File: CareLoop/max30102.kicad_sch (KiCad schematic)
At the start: 4 parts, among them U2 MAX30102

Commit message: updated version
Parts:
- added C21, C22: 4.7u, Capacitor_SMD:C_0603_1608Metric_Pad1.08x0.95mm_HandSolder, symbol Device:C
- added C23: 100n, Capacitor_SMD:C_0603_1608Metric_Pad1.08x0.95mm_HandSolder, symbol Device:C
- added C24: 1u, Capacitor_SMD:C_0603_1608Metric_Pad1.08x0.95mm_HandSolder, symbol Device:C
- added R8: 10k, Resistor_SMD:R_0603_1608Metric_Pad0.98x0.95mm_HandSolder, symbol Device:R
- added U1: MCP1727-1802xMF, Package_DFN_QFN:DFN-8-1EP_3x3mm_P0.65mm_EP1.55x2.4mm, symbol Regulator_Linear:MCP1727-1802xMF
- C3: value 1u -> 10u
- renumbered JP1 to JP1_MAX30102
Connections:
- net GND: now also C21.2, C22.2, C23.2, C24.2, U1.4 (GND), U1.9 (GND)
- net at C15.1, C3.1, JP1_MAX30102.1 (A)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: now also C22.1, C23.1, R8.1, U1.1 (Vin), U1.2 (Vin), U1.3 (~{SHDN}); no longer U2.11 (VDD)
- net MAX_INT: now reaches U2.13 (~{INT})
- net MAX_INT: now also R8.2
- new net: C21.1, C24.1, U1.8 (Vout), U2.11 (VDD)
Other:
- moved on the sheet: JP1_MAX30102

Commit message: WP: update Schematics
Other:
- moved on the sheet: C15, C21, C22, C23, C24, C3, JP1_MAX30102, R8, U1, U2

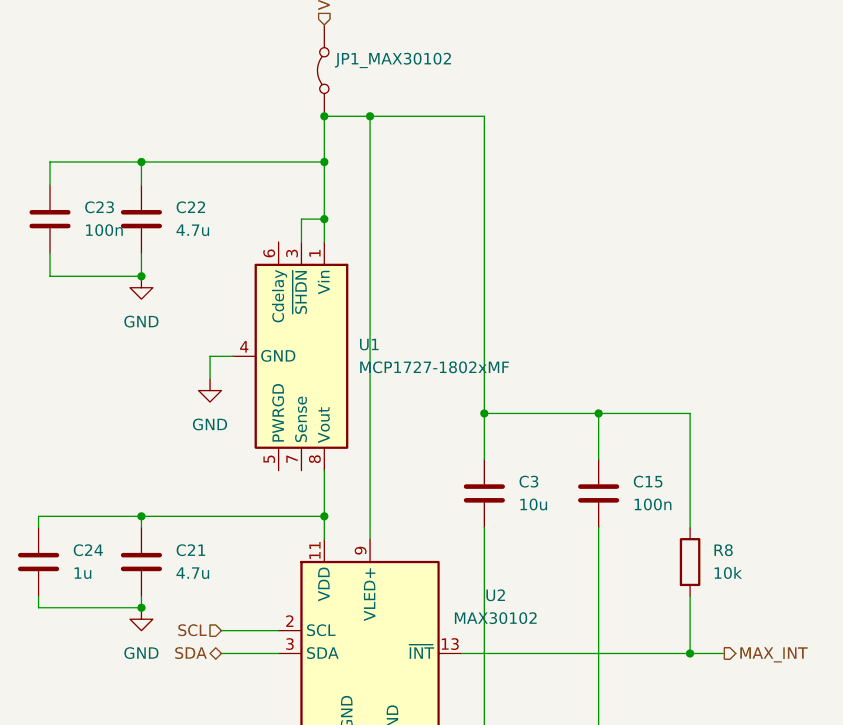
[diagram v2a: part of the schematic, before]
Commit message: WP: Placement PCB Parts done
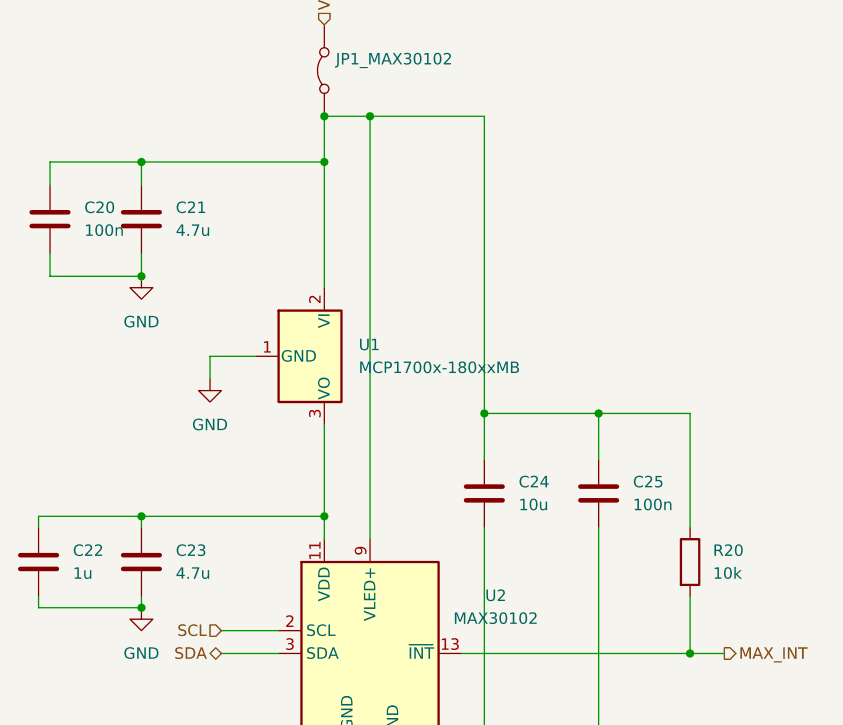
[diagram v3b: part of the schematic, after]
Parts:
- removed U1: MCP1727-1802xMF, Package_DFN_QFN:DFN-8-1EP_3x3mm_P0.65mm_EP1.55x2.4mm, symbol Regulator_Linear:MCP1727-1802xMF
- added U1: MCP1700x-180xxMB, Package_TO_SOT_SMD:SOT-89-3, symbol Regulator_Linear:MCP1700x-180xxMB
- C20: renamed from C23; footprint Capacitor_SMD:C_0603_1608Metric_Pad1.08x0.95mm_HandSolder -> Capacitor_SMD:C_0201_0603Metric_Pad0.64x0.40mm_HandSolder
- C21: renamed from C22; footprint Capacitor_SMD:C_0603_1608Metric_Pad1.08x0.95mm_HandSolder -> Capacitor_SMD:C_0402_1005Metric_Pad0.74x0.62mm_HandSolder
- C22: renamed from C24; footprint Capacitor_SMD:C_0603_1608Metric_Pad1.08x0.95mm_HandSolder -> Capacitor_SMD:C_0402_1005Metric_Pad0.74x0.62mm_HandSolder
- C23: renamed from C21; footprint Capacitor_SMD:C_0603_1608Metric_Pad1.08x0.95mm_HandSolder -> Capacitor_SMD:C_0402_1005Metric_Pad0.74x0.62mm_HandSolder
- C24: renamed from C3; footprint Capacitor_SMD:C_0603_1608Metric_Pad1.08x0.95mm_HandSolder -> Capacitor_SMD:C_0402_1005Metric_Pad0.74x0.62mm_HandSolder
- C25: renamed from C15; footprint Capacitor_SMD:C_0603_1608Metric_Pad1.08x0.95mm_HandSolder -> Capacitor_SMD:C_0201_0603Metric_Pad0.64x0.40mm_HandSolder
- R20: renamed from R8; footprint Resistor_SMD:R_0603_1608Metric_Pad0.98x0.95mm_HandSolder -> Resistor_SMD:R_0402_1005Metric_Pad0.72x0.64mm_HandSolder
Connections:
- net GND: now also U1.1 (GND)
- net at C20.1, C21.1, C24.1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: now also U1.2 (VI)
- net at C22.1, C23.1, U2.11 (VDD): now also U1.3 (VO)
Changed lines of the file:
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@@
 		(color 0 0 0 0)
 	)
-	(junction
-		(at 138.43 60.96)
-		(diameter 0)
-		(color 0 0 0 0)
-	)
 	(wire
 		(pts
@@
 	(wire
 		(pts
-			(xy 138.43 88.9) (xy 138.43 93.98)
-		)
-		(stroke
-			(width 0)
-			(type default)
-		)
-	)
-	(wire
-		(pts
-			(xy 138.43 60.96) (xy 138.43 63.5)
+			(xy 138.43 54.61) (xy 138.43 68.58)
 		)
 		(stroke
@@
 	(wire
 		(pts
-			(xy 135.89 60.96) (xy 138.43 60.96)
-		)
-		(stroke
-			(width 0)
-			(type default)
-		)
-	)
-	(wire
-		(pts
 			(xy 179.07 109.22) (xy 182.88 109.22)
 		)
@@
 	(wire
 		(pts
-			(xy 138.43 54.61) (xy 138.43 60.96)
+			(xy 138.43 83.82) (xy 138.43 93.98)
 		)
 		(stroke
@@
 	(wire
 		(pts
-			(xy 125.73 76.2) (xy 128.27 76.2)
+			(xy 125.73 76.2) (xy 130.81 76.2)
 		)
 		(stroke
@@
 		(pts
 			(xy 168.91 82.55) (xy 168.91 87.63)
-		)
-		(stroke
-			(width 0)
-			(type default)
-		)
-	)
-	(wire
-		(pts
-			(xy 135.89 63.5) (xy 135.89 60.96)
 		)
 		(stroke
@@
 			)
 			(justify left)
+		)
+	)
+	(symbol
+		(lib_id "Regulator_Linear:MCP1700x-180xxMB")
+		(at 138.43 76.2 270)
+		(unit 1)
+		(exclude_from_sim no)
+		(in_bom yes)
+		(on_board yes)
+		(dnp no)
+		(fields_autoplaced yes)
+		(property "Reference" "U1"
+			(at 142.24 74.9299 90)
+			(effects
+				(font
+					(size 1.27 1.27)
+				)
+				(justify left)
+			)
+		)
+		(property "Value" "MCP1700x-180xxMB"
+			(at 142.24 77.4699 90)
+			(effects
+				(font
+					(size 1.27 1.27)
+				)
+				(justify left)
+			)
+		)
+		(property "Footprint" "Package_TO_SOT_SMD:SOT-89-3"
+			(at 143.51 76.2 0)
+			(effects
+				(font
+					(size 1.27 1.27)
+				)
+				(hide yes)
+			)
+		)
+		(property "Datasheet" "http://ww1.microchip.com/downloads/en/DeviceDoc/20001826D.pdf"
+			(at 137.16 76.2 0)
+			(effects
+				(font
+					(size 1.27 1.27)
+				)
+				(hide yes)
+			)
+		)
+		(property "Description" "250mA Low Quiscent Current LDO, 1.8V output, SOT-89"
+			(at 138.43 76.2 0)
+			(effects
+				(font
+					(size 1.27 1.27)
+				)
+				(hide yes)
+			)
+		)
+		(pin "3"
+		)
+		(pin "2"
+		)
+		(pin "1"
+		)
+		(instances
+			(project ""
+				(path "/1249f778-de2d-49b4-b768-08b76b87278f/b38cd729-7350-45f3-a38f-570d6a1e3d63"
+					(reference "U1")
+					(unit 1)
+				)
+			)
 		)
 	)
@@
 		(dnp no)
 		(fields_autoplaced yes)
-		(property "Reference" "C23"
+		(property "Reference" "C20"
 			(at 111.76 59.6899 0)
 			(effects
@@
 			)
 		)
-		(property "Footprint" "Capacitor_SMD:C_0603_1608Metric_Pad1.08x0.95mm_HandSolder"
+		(property "Footprint" "Capacitor_SMD:C_0201_0603Metric_Pad0.64x0.40mm_HandSolder"
 			(at 108.9152 64.77 0)
 			(effects
@@
 			(project "CareLoop_PCB"
 				(path "/1249f778-de2d-49b4-b768-08b76b87278f/b38cd729-7350-45f3-a38f-570d6a1e3d63"
-					(reference "C23")
+					(reference "C20")
 					(unit 1)
 				)
@@
 	)
 	(symbol
-		(lib_id "Regulator_Linear:MCP1727-1802xMF")
-		(at 135.89 76.2 270)
-		(unit 1)
-		(exclude_from_sim no)
-		(in_bom yes)
-		(on_board yes)
-		(dnp no)
-		(fields_autoplaced yes)
-		(property "Reference" "U1"
-			(at 142.24 74.9299 90)
-			(effects
-				(font
-					(size 1.27 1.27)
-				)
-				(justify left)
-			)
-		)
-		(property "Value" "MCP1727-1802xMF"
-			(at 142.24 77.4699 90)
-			(effects
-				(font
-					(size 1.27 1.27)
-				)
-				(justify left)
-			)
-		)
-		(property "Footprint" "Package_DFN_QFN:DFN-8-1EP_3x3mm_P0.65mm_EP1.55x2.4mm"
-			(at 160.02 76.2 0)
-			(effects
-				(font
-					(size 1.27 1.27)
-				)
-				(hide yes)
-			)
-		)
-		(property "Datasheet" "https://ww1.microchip.com/downloads/aemtest/APID/ProductDocuments/DataSheets/MCP1727-1.5A-Low-Voltage-Low-Quiescent-Current-LDO-Regulator-20001999D.pdf"
-			(at 157.48 76.2 0)
-			(effects
-				(font
-					(size 1.27 1.27)
-				)
-				(hide yes)
-			)
-		)
-		(property "Description" "1.5A, Low Voltage, Low Quiescent Current LDO Regulator, 2.3 - 6V Input, Fixed 1.8V Output, 330mV Dropout, DFN-8"
-			(at 135.89 76.2 0)
-			(effects
-				(font
-					(size 1.27 1.27)
-				)
-				(hide yes)
-			)
-		)
-		(pin "7"
-		)
-		(pin "5"
-		)
-		(pin "1"
-		)
-		(pin "6"
-		)
-		(pin "8"
-		)
-		(pin "2"
-		)
-		(pin "3"
-		)
-		(pin "4"
-		)
-		(pin "9"
-		)
-		(instances
-			(project ""
-				(path "/1249f778-de2d-49b4-b768-08b76b87278f/b38cd729-7350-45f3-a38f-570d6a1e3d63"
-					(reference "U1")
-					(unit 1)
-				)
-			)
-		)
-	)
-	(symbol
 		(lib_id "Device:C")
 		(at 168.91 91.44 0)
@@
 		(dnp no)
 		(fields_autoplaced yes)
-		(property "Reference" "C15"
+		(property "Reference" "C25"
 			(at 172.72 90.1699 0)
 			(effects
@@
 			)
 		)
-		(property "Footprint" "Capacitor_SMD:C_0603_1608Metric_Pad1.08x0.95mm_HandSolder"
+		(property "Footprint" "Capacitor_SMD:C_0201_0603Metric_Pad0.64x0.40mm_HandSolder"
 			(at 169.8752 95.25 0)
 			(effects
@@
 			(project ""
 				(path "/1249f778-de2d-49b4-b768-08b76b87278f/b38cd729-7350-45f3-a38f-570d6a1e3d63"
-					(reference "C15")
+					(reference "C25")
 					(unit 1)
 				)
@@
 		(dnp no)
 		(fields_autoplaced yes)
-		(property "Reference" "C3"
+		(property "Reference" "C24"
 			(at 160.02 90.1699 0)
 			(effects
@@
 			)
 		)
-		(property "Footprint" "Capacitor_SMD:C_0603_1608Metric_Pad1.08x0.95mm_HandSolder"
+		(property "Footprint" "Capacitor_SMD:C_0402_1005Metric_Pad0.74x0.62mm_HandSolder"
 			(at 157.1752 95.25 0)
 			(effects
@@
 			(project "CareLoop_PCB"
 				(path "/1249f778-de2d-49b4-b768-08b76b87278f/b38cd729-7350-45f3-a38f-570d6a1e3d63"
-					(reference "C3")
+					(reference "C24")
 					(unit 1)
 				)
@@
 		(dnp no)
 		(fields_autoplaced yes)
-		(property "Reference" "C22"
+		(property "Reference" "C21"
 			(at 121.92 59.6899 0)
 			(effects
@@
 			)
 		)
-		(property "Footprint" "Capacitor_SMD:C_0603_1608Metric_Pad1.08x0.95mm_HandSolder"
+		(property "Footprint" "Capacitor_SMD:C_0402_1005Metric_Pad0.74x0.62mm_HandSolder"
 			(at 119.0752 64.77 0)
 			(effects
@@
 			(project "CareLoop_PCB"
 				(path "/1249f778-de2d-49b4-b768-08b76b87278f/b38cd729-7350-45f3-a38f-570d6a1e3d63"
-					(reference "C22")
+					(reference "C21")
 					(unit 1)
 				)
@@
 		(dnp no)
 		(fields_autoplaced yes)
-		(property "Reference" "C21"
+		(property "Reference" "C23"
 			(at 121.92 97.7899 0)
 			(effects
@@
 			)
 		)
-		(property "Footprint" "Capacitor_SMD:C_0603_1608Metric_Pad1.08x0.95mm_HandSolder"
+		(property "Footprint" "Capacitor_SMD:C_0402_1005Metric_Pad0.74x0.62mm_HandSolder"
 			(at 119.0752 102.87 0)
 			(effects
@@
 			(project "CareLoop_PCB"
 				(path "/1249f778-de2d-49b4-b768-08b76b87278f/b38cd729-7350-45f3-a38f-570d6a1e3d63"
-					(reference "C21")
+					(reference "C23")
 					(unit 1)
 				)
@@
 		(dnp no)
 		(fields_autoplaced yes)
-		(property "Reference" "C24"
+		(property "Reference" "C22"
 			(at 110.49 97.7899 0)
 			(effects
@@
 			)
 		)
-		(property "Footprint" "Capacitor_SMD:C_0603_1608Metric_Pad1.08x0.95mm_HandSolder"
+		(property "Footprint" "Capacitor_SMD:C_0402_1005Metric_Pad0.74x0.62mm_HandSolder"
 			(at 107.6452 102.87 0)
 			(effects
@@
 			(project "CareLoop_PCB"
 				(path "/1249f778-de2d-49b4-b768-08b76b87278f/b38cd729-7350-45f3-a38f-570d6a1e3d63"
-					(reference "C24")
+					(reference "C22")
 					(unit 1)
 				)
@@
 		(dnp no)
 		(fields_autoplaced yes)
-		(property "Reference" "R8"
+		(property "Reference" "R20"
 			(at 181.61 97.7899 0)
 			(effects
@@
 			)
 		)
-		(property "Footprint" "Resistor_SMD:R_0603_1608Metric_Pad0.98x0.95mm_HandSolder"
+		(property "Footprint" "Resistor_SMD:R_0402_1005Metric_Pad0.72x0.64mm_HandSolder"
 			(at 177.292 99.06 90)
 			(effects
@@
 			(project ""
 				(path "/1249f778-de2d-49b4-b768-08b76b87278f/b38cd729-7350-45f3-a38f-570d6a1e3d63"
-					(reference "R8")
+					(reference "R20")
 					(unit 1)
 				)

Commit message: WP: updatet version with routing
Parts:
- added C26: 100p, Capacitor_SMD:C_0201_0603Metric_Pad0.64x0.40mm_HandSolder, symbol Device:C_Small
- added C27: 100n, Capacitor_SMD:C_0201_0603Metric_Pad0.64x0.40mm_HandSolder, symbol Device:C_Small
- added R21: 200k, Resistor_SMD:R_0402_1005Metric_Pad0.72x0.64mm_HandSolder, symbol Device:R
- added R22, R23: 4k7, Resistor_SMD:R_0402_1005Metric_Pad0.72x0.64mm_HandSolder, symbol Device:R
- added U7: PCA9306, Package_SON:X2SON-8_1.4x1mm_P0.35mm, symbol Interface:PCA9306
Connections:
- net GND: now also C26.1, C27.1, U7.1 (GND)
- net SCL: now also U7.6 (SCL2); no longer U2.2 (SCL)
- net SDA: now also U7.5 (SDA2); no longer U2.3 (SDA)
- net VCC: now also R21.2
- net at C22.1, C23.1, U1.3 (VO)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: now also R22.1, R23.1, U7.2 (VREF1)
- new net: C26.2, C27.2, R21.1, U7.7 (VREF2), U7.8 (EN)
- new net: R22.2, U2.2 (SCL), U7.3 (SCL1)
- new net: R23.2, U2.3 (SDA), U7.4 (SDA1)
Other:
- moved on the sheet: C22, C23

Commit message: update routing
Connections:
- net VCC: now also R20.1
- net at C20.1, C21.1, C24.1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: no longer R20.1
- net VCC_1.8V: now reaches C22.1, C23.1, R22.1, R23.1, U1.3 (VO), U2.11 (VDD), U7.2 (VREF1)
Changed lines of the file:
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@@
+	)
+	(junction
+		(at 138.43 86.36)
+		(diameter 0)
+		(color 0 0 0 0)
 	)
 	(junction
@@
 	)
 	(junction
-		(at 168.91 82.55)
-		(diameter 0)
-		(color 0 0 0 0)
-	)
-	(junction
 		(at 143.51 49.53)
 		(diameter 0)
@@
 	(wire
 		(pts
-			(xy 179.07 82.55) (xy 179.07 95.25)
-		)
-		(stroke
-			(width 0)
-			(type default)
-		)
-	)
-	(wire
-		(pts
 			(xy 106.68 109.22) (xy 125.73 109.22)
 		)
@@
 	(wire
 		(pts
-			(xy 179.07 82.55) (xy 168.91 82.55)
-		)
-		(stroke
-			(width 0)
-			(type default)
-		)
-	)
-	(wire
-		(pts
 			(xy 106.68 87.63) (xy 110.49 87.63)
 		)
@@
 	(wire
 		(pts
-			(xy 138.43 83.82) (xy 138.43 87.63)
+			(xy 138.43 83.82) (xy 138.43 86.36)
 		)
 		(stroke
@@
 	(wire
 		(pts
+			(xy 179.07 91.44) (xy 179.07 95.25)
+		)
+		(stroke
+			(width 0)
+			(type default)
+		)
+	)
+	(wire
+		(pts
 			(xy 110.49 87.63) (xy 110.49 95.25)
 		)
@@
 	(wire
 		(pts
+			(xy 135.89 86.36) (xy 138.43 86.36)
+		)
+		(stroke
+			(width 0)
+			(type default)
+		)
+	)
+	(wire
+		(pts
 			(xy 129.54 100.33) (xy 129.54 99.06)
 		)
@@
 		(pts
 			(xy 113.03 111.76) (xy 133.35 111.76)
+		)
+		(stroke
+			(width 0)
+			(type default)
+		)
+	)
+	(wire
+		(pts
+			(xy 138.43 86.36) (xy 138.43 87.63)
 		)
 		(stroke
@@
 		)
 	)
+	(hierarchical_label "VCC_1.8V"
+		(shape input)
+		(at 135.89 86.36 180)
+		(effects
+			(font
+				(size 1.27 1.27)
+			)
+			(justify right)
+		)
+	)
+	(hierarchical_label "VCC"
+		(shape input)
+		(at 179.07 91.44 90)
+		(effects
+			(font
+				(size 1.27 1.27)
+			)
+			(justify left)
+		)
+	)

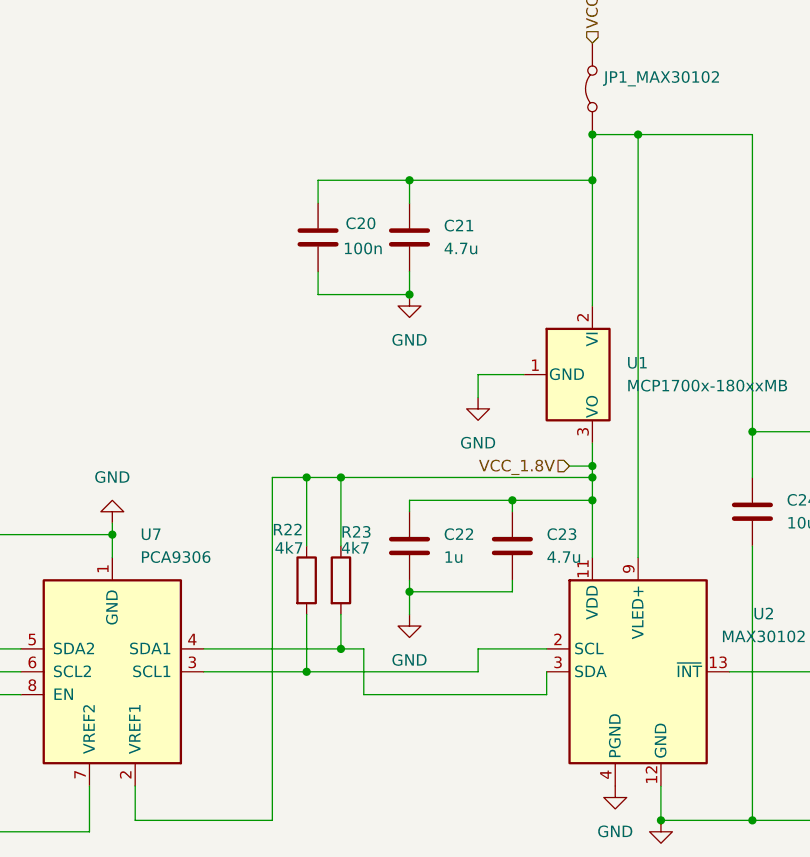
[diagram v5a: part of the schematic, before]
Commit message: updated vias
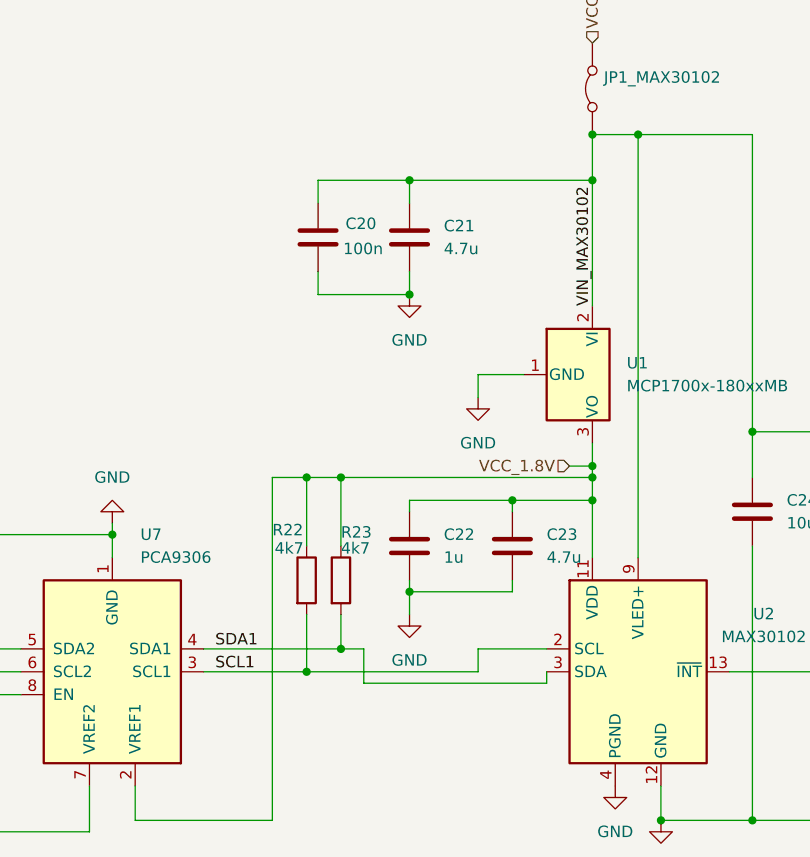
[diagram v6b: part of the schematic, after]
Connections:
- net VIN_MAX30102: now reaches C20.1, C21.1, C24.1, C25.1, JP1_MAX30102.1 (A), U1.2 (VI), U2.10 (VLED+), U2.9 (VLED+)
- net SCL1: now reaches R22.2, U2.2 (SCL), U7.3 (SCL1)
- net SDA1: now reaches R23.2, U2.3 (SDA), U7.4 (SDA1)
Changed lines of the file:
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@@
 	(wire
 		(pts
-			(xy 113.03 106.68) (xy 113.03 111.76)
+			(xy 113.03 106.68) (xy 113.03 110.49)
 		)
 		(stroke
@@
 	(wire
 		(pts
-			(xy 133.35 111.76) (xy 133.35 109.22)
+			(xy 133.35 110.49) (xy 133.35 109.22)
 		)
 		(stroke
@@
 	(wire
 		(pts
-			(xy 113.03 111.76) (xy 133.35 111.76)
+			(xy 113.03 110.49) (xy 133.35 110.49)
 		)
 		(stroke
@@
 		)
 	)
+	(label "SDA1"
+		(at 96.52 106.68 0)
+		(effects
+			(font
+				(size 1.27 1.27)
+			)
+			(justify left bottom)
+		)
+	)
+	(label "VIN_MAX30102"
+		(at 138.43 68.58 90)
+		(effects
+			(font
+				(size 1.27 1.27)
+			)
+			(justify left bottom)
+		)
+	)
+	(label "SCL1"
+		(at 96.52 109.22 0)
+		(effects
+			(font
+				(size 1.27 1.27)
+			)
+			(justify left bottom)
+		)
+	)
